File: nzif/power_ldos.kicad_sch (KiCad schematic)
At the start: 62 parts, among them U152 LT3042xMSE, U153 LT3042xMSE, U154 LT3042xMSE, U155 LT3042xMSE, U156 LT3042xMSE, U157 LT3042xMSE, U158 LT3045xMSE, U159 LT3045xMSE, U160 LT3045xMSE, U161 LT3045xMSE, U162 LT3045xMSE, U163 LT3045xMSE, U164 LT3045xMSE

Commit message: Digikey parts for rcv stages
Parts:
- C324, C325, C335: Digikey Part # (none) -> 587-3258-1-ND
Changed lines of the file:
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@@
 			)
 		)
-		(property "Datasheet" "~"
+		(property "Datasheet" "https://mm.digikey.com/Volume0/opasdata/d220001/medias/docus/1231/LMK107BBJ106MALT_SS.pdf"
 			(at 228.6 35.56 0)
 			(effects
@@
 			)
 		)
-		(property "Digikey Part #" ""
+		(property "Digikey Part #" "587-3258-1-ND"
 			(at 228.6 35.56 0)
 			(effects
@@
 			)
 		)
-		(property "Datasheet" "~"
+		(property "Datasheet" "https://mm.digikey.com/Volume0/opasdata/d220001/medias/docus/1231/LMK107BBJ106MALT_SS.pdf"
 			(at 326.39 35.56 0)
 			(effects
@@
 			)
 		)
-		(property "Digikey Part #" ""
+		(property "Digikey Part #" "587-3258-1-ND"
 			(at 326.39 35.56 0)
 			(effects
@@
 			)
 		)
-		(property "Datasheet" "~"
+		(property "Datasheet" "https://mm.digikey.com/Volume0/opasdata/d220001/medias/docus/1231/LMK107BBJ106MALT_SS.pdf"
 			(at 226.06 113.03 0)
 			(effects
@@
 			)
 		)
-		(property "Digikey Part #" ""
+		(property "Digikey Part #" "587-3258-1-ND"
 			(at 226.06 113.03 0)
 			(effects

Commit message: add annotations - first run of erc
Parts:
- renumbered C306 to C312, C307 to C313, C308 to C314, C310 to C315, C309 to C316, C311 to C317, C312 to C318, C313 to C319, C314 to C320, C315 to C321, C316 to C322, C317 to C323, C318 to C324, C319 to C325, C320 to C326, C321 to C327, C322 to C328, C323 to C329, C324 to C330, C325 to C331, C326 to C332, C327 to C333, C328 to C334, C329 to C335, C330 to C336, C331 to C337, C332 to C338, C333 to C339, C334 to C340, C335 to C341, C336 to C342, C337 to C343, C338 to C344, R226 to R194, R225 to R195, R227 to R196, R228 to R197, R229 to R198, R230 to R199, R231 to R200, R232 to R201, R233 to R202, R234 to R203, R235 to R204, R236 to R205, R237 to R206, R238 to R207, R239 to R208, R240 to R209, U152 to U144, U153 to U145, U154 to U146, U155 to U147, U156 to U148, U157 to U149, U158 to U150, U159 to U151, U160 to U152, U161 to U153, U162 to U154, U163 to U155, U164 to U156

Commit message: updated power on all schematics
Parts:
- removed C330, C331: 10u, Capacitor_SMD:C_0603_1608Metric_Pad1.08x0.95mm_HandSolder, symbol Device:C_Small
- removed C332, C333, C335: 0.47u, Capacitor_SMD:C_0603_1608Metric_Pad1.08x0.95mm_HandSolder, symbol Device:C_Small
- removed C334, C336, C337, C338, C339, C340: 4.7u, Capacitor_SMD:C_0603_1608Metric_Pad1.08x0.95mm_HandSolder, symbol Device:C_Small
- removed R200, R201: 16.5k, Resistor_SMD:R_0603_1608Metric_Pad0.98x0.95mm_HandSolder, symbol Device:R_Small_US
- removed R202: 33.2k, Resistor_SMD:R_0603_1608Metric_Pad0.98x0.95mm_HandSolder, symbol Device:R_Small_US
- removed R203, R204, R205, R206: 20m, Resistor_SMD:R_0603_1608Metric_Pad0.98x0.95mm_HandSolder, symbol Device:R_Small_US
- removed U144, U145, U146, U147, U148, U149: LT3042xMSE, Package_SO:MSOP-10-1EP_3x3mm_P0.5mm_EP1.68x1.88mm, symbol Regulator_Linear:LT3042xMSE
- removed U150, U151, U152, U154: LT3045xMSE, Package_SO:MSOP-12-1EP_3x4.039mm_P0.65mm_EP1.651x2.845mm, symbol Regulator_Linear:LT3045xMSE
- added C? (x2): 4.7u, Capacitor_SMD:C_0603_1608Metric_Pad1.08x0.95mm_HandSolder, symbol Device:C_Small
- added C?: 0.47u, Capacitor_SMD:C_0603_1608Metric_Pad1.08x0.95mm_HandSolder, symbol Device:C_Small
- added R?: 49.9, Resistor_SMD:R_0603_1608Metric_Pad0.98x0.95mm_HandSolder, symbol Device:R_Small_US
- added U144, U145, U146, U147, U148, U149: LT3045xMSE, Package_SO:MSOP-12-1EP_3x4.039mm_P0.65mm_EP1.651x2.845mm, symbol Regulator_Linear:LT3045xMSE
- C323, C327: value 4.7u -> 0.47u
- C324, C326: value 0.47u -> 4.7u
- R197: value 33.2k -> 49.9
- R199: value 49.9 -> 49.9k
- renumbered U153 to U?
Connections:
- net 3.3V_DACs is gone; now on an unnamed net: C327.1
- net 5V_RX_OPAMPS is gone; now on net +6.5V_RX_OPAMPS: C320.1
- net GND: now also C?.2, C?.2, C?.2, R?.2, U144.13 (GND), U144.6 (ILIM), U144.9 (GND), U145.13 (GND), U145.6 (ILIM), U145.9 (GND), U146.13 (GND), U146.6 (ILIM), U146.9 (GND), U147.13 (GND), U147.6 (ILIM), U147.9 (GND), U148.13 (GND), U148.6 (ILIM), U148.9 (GND), U149.13 (GND), U149.6 (ILIM), U149.9 (GND)
- net at C317.1, R196.1: now also U?.8 (SET)
- net at R199.1: now also U149.8 (SET); no longer C326.1
- net at R197.1: now also C323.1, U147.8 (SET); no longer C324.1
- net at C316.1, R195.1: now also U148.8 (SET)
- net at C315.1, R194.1: now also U145.8 (SET)
- net at C325.1, R198.1: now also U144.8 (SET)
- net +6.5V_RX_OPAMPS: now reaches U?.10 (OUTS), U?.11 (OUT), U?.12 (OUT)
- net 3.3V_ADCs renamed +3.3V_CONVERTERS
- net +3.3V_CONVERTERS: now also U148.10 (OUTS), U148.11 (OUT), U148.12 (OUT)
- net 3.3V_DSP renamed +3.3V_DSP_UC
- net 3.6V renamed 4V
- net 4V: now also C?.1, U146.1 (IN), U146.2 (IN), U146.3 (IN), U146.4 (EN/UV), U146.7 (PGFB), U147.1 (IN), U147.2 (IN), U147.3 (IN), U147.4 (EN/UV), U147.7 (PGFB), U148.1 (IN), U148.2 (IN), U148.3 (IN), U148.4 (EN/UV), U148.7 (PGFB); no longer C314.1, U?.1 (IN), U?.2 (IN), U?.3 (IN), U?.4 (EN/UV), U?.7 (PGFB)
- net 5.5V renamed 6V
- net 6V: now also C326.1, U144.1 (IN), U144.2 (IN), U144.3 (IN), U144.4 (EN/UV), U144.7 (PGFB), U145.1 (IN), U145.2 (IN), U145.3 (IN), U145.4 (EN/UV), U145.7 (PGFB), U149.1 (IN), U149.2 (IN), U149.3 (IN), U149.4 (EN/UV), U149.7 (PGFB); no longer C323.1
- net 5V_RX_Mixer renamed +5V_RX_MIXER
- net +5V_RX_MIXER: now also U145.10 (OUTS), U145.11 (OUT), U145.12 (OUT)
- net 5V_TX_Mixer renamed +5V_TX_MIXER
- net +5V_TX_MIXER: now also U144.10 (OUTS), U144.11 (OUT), U144.12 (OUT)
- net 5V_TX_OPAMPS renamed +5V_LOUDSPEAKER
- net +5V_LOUDSPEAKER: now also U149.10 (OUTS), U149.11 (OUT), U149.12 (OUT)
- new net: C?.1, R?.1, U146.8 (SET)
- new net +1.8V_CLOCKTREE: C?.1, U146.10 (OUTS), U146.11 (OUT), U146.12 (OUT)
- new net +3.3V_CLOCKTREE: C324.1, U147.10 (OUTS), U147.11 (OUT), U147.12 (OUT)
- new net 8V: C314.1, U?.1 (IN), U?.2 (IN), U?.3 (IN), U?.4 (EN/UV), U?.7 (PGFB)
- no-connect marks 13 -> 9
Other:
- note added: "3.3V Power for ADCs/DACs/Codec"
- note added: "3.3V Power for DSP and uC"
- note added: "5V Power for Loudspeaker"
- note added: "6.5V Power for RX op amps"
- note added: "Resistor sets 1.8V output Use high quality cap such as COG"
- note added: "Resistor sets 6.5V output Use high quality cap such as COG"
- note removed: "3.3V Power for ADCs"
- note removed: "3.3V Power for DACs"
- note removed: "3.3V Power for DSP"
- note removed: "3.3V Power for Microcontroller"
- note removed: "5V Power for RX op amps"
- note removed: "5V Power for TX Op amps"
- moved on the sheet: U?

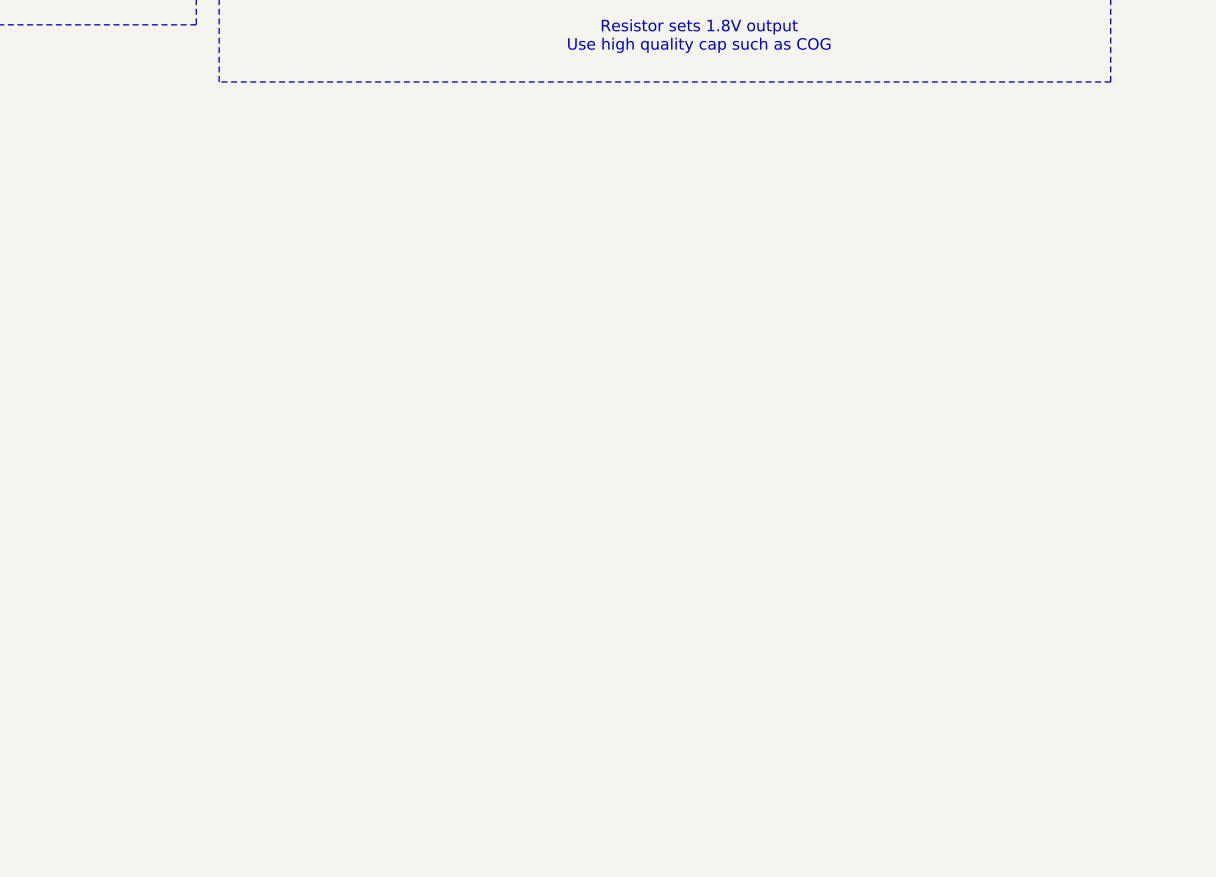
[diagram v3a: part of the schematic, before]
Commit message: added ldo for 2.5V
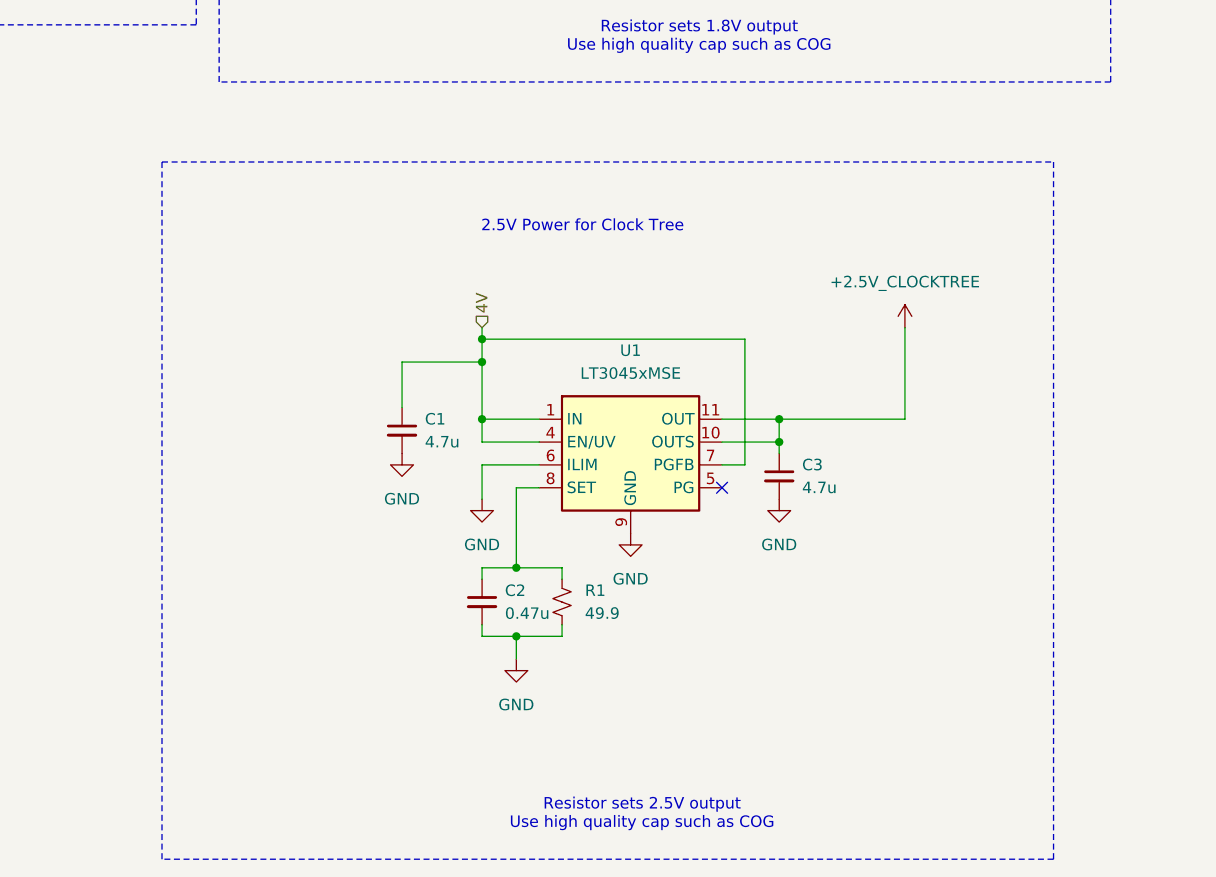
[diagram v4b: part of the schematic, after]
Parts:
- added C1, C3: 4.7u, Capacitor_SMD:C_0603_1608Metric_Pad1.08x0.95mm_HandSolder, symbol Device:C_Small
- added C2: 0.47u, Capacitor_SMD:C_0603_1608Metric_Pad1.08x0.95mm_HandSolder, symbol Device:C_Small
- added R1: 49.9, Resistor_SMD:R_0603_1608Metric_Pad0.98x0.95mm_HandSolder, symbol Device:R_Small_US
- added U1: LT3045xMSE, Package_SO:MSOP-12-1EP_3x4.039mm_P0.65mm_EP1.651x2.845mm, symbol Regulator_Linear:LT3045xMSE
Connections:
- net 4V: now also C1.1, U1.1 (IN), U1.2 (IN), U1.3 (IN), U1.4 (EN/UV), U1.7 (PGFB)
- net GND: now also C1.2, C2.2, C3.2, R1.2, U1.13 (GND), U1.6 (ILIM), U1.9 (GND)
- new net: C2.1, R1.1, U1.8 (SET)
- new net +2.5V_CLOCKTREE: C3.1, U1.10 (OUTS), U1.11 (OUT), U1.12 (OUT)
- no-connect marks 9 -> 10
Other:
- note added: "2.5V Power for Clock Tree"
- note added: "Resistor sets 2.5V output Use high quality cap such as COG"

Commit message: cartoons on main2
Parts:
- renumbered C1 to C?, C3 to C?, C2 to C?, R1 to R?, U1 to U?

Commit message: wire top sheet from rf front end through rx driver amps
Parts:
- gave numbers to parts that had none: 10
- renumbered C312 to C901, C313 to C902, C314 to C903, C315 to C904, C316 to C905, C317 to C906, C318 to C907, C319 to C908, C320 to C909, C322 to C910, C326 to C911, C325 to C912, C327 to C913, C328 to C914, C329 to C915, C321 to C917, C323 to C920, C324 to C923, C341 to C925, C342 to C926, C343 to C927, C344 to C928, R194 to R901, R195 to R902, R196 to R903, R198 to R904, R199 to R905, R197 to R907, R207 to R909, R208 to R910, R209 to R911, U148 to U901, U145 to U902, U144 to U904, U149 to U905, U147 to U907, U146 to U908, U155 to U909, U156 to U910

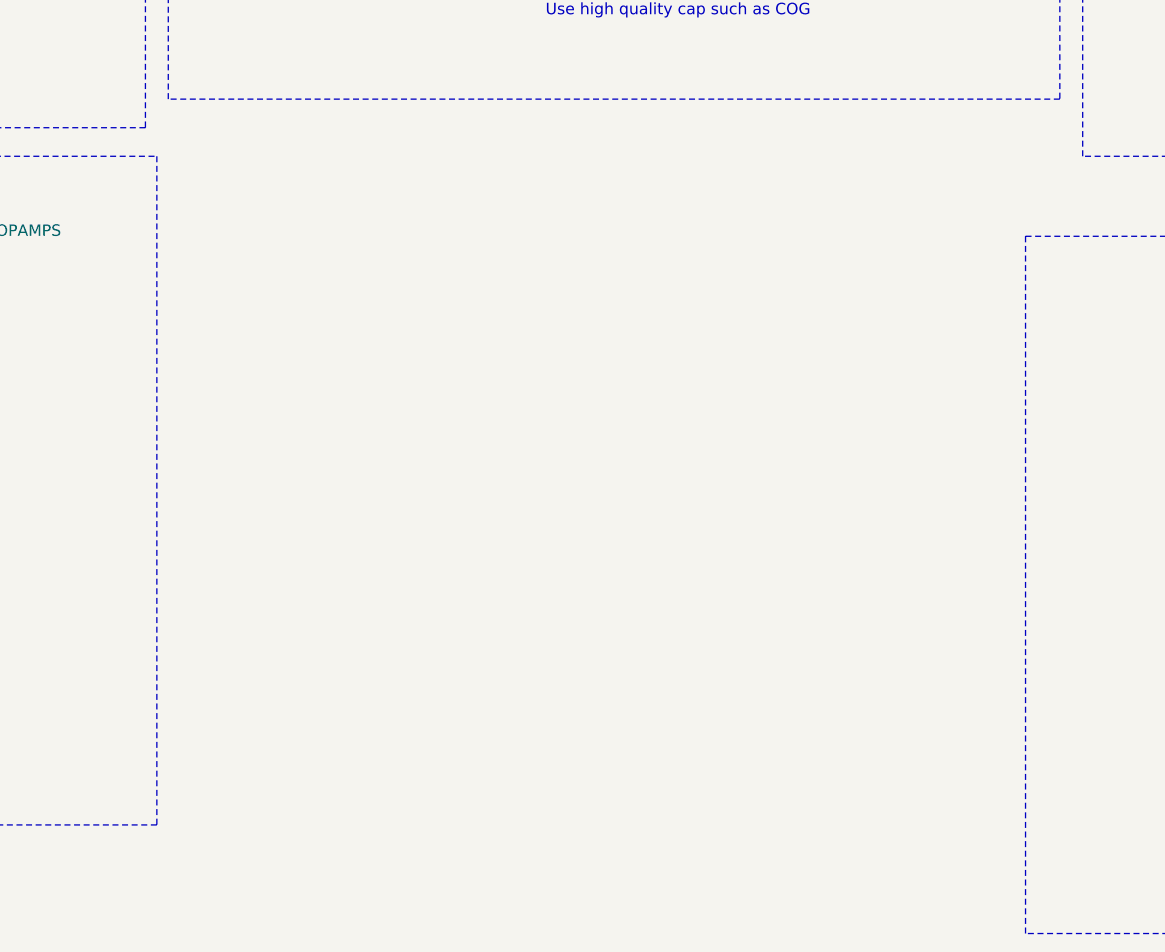
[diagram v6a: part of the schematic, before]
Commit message: added -3.5V rail
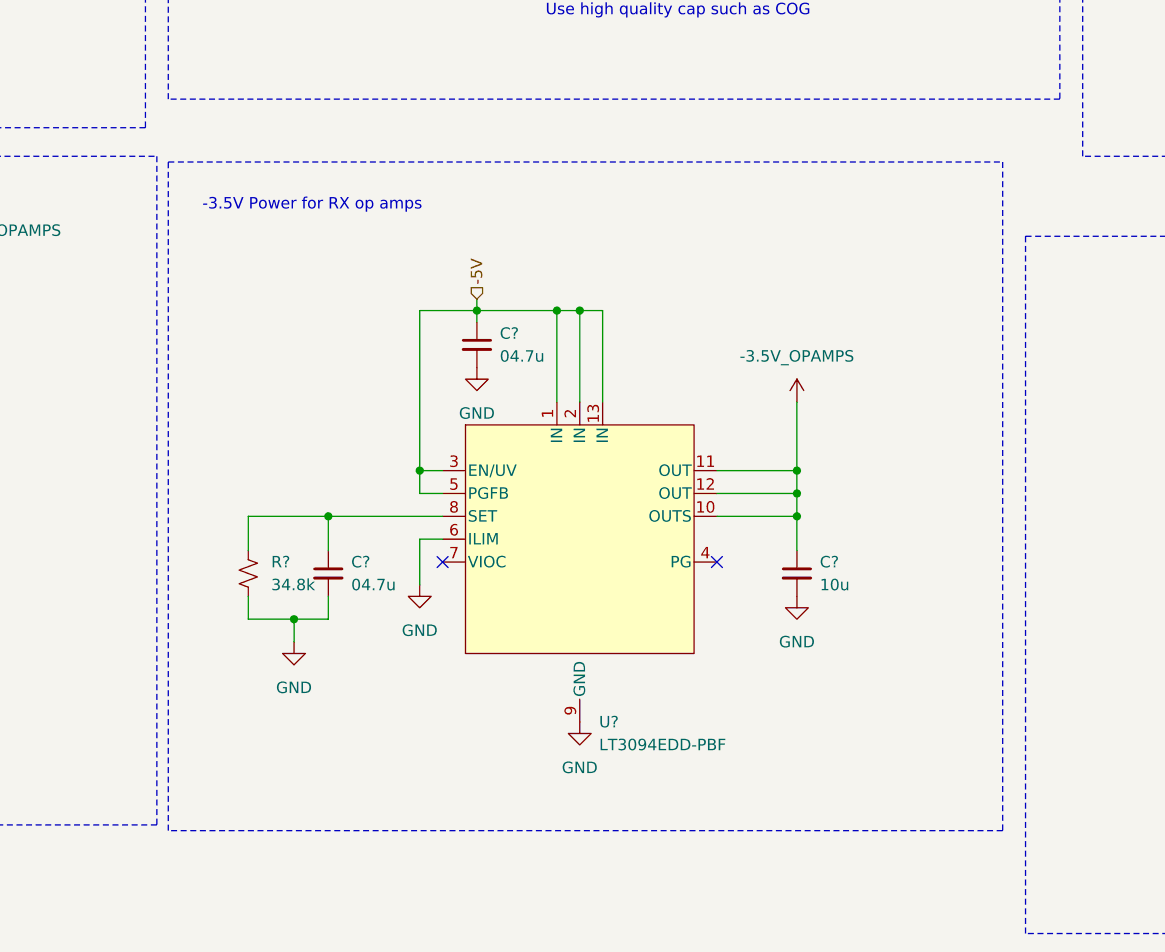
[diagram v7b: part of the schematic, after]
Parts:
- added C?: 10u, Capacitor_SMD:C_0603_1608Metric_Pad1.08x0.95mm_HandSolder, symbol Device:C_Small
- added C? (x2): 04.7u, Capacitor_SMD:C_0603_1608Metric_Pad1.08x0.95mm_HandSolder, symbol Device:C_Small
- added R?: 34.8k, symbol Device:R_Small_US
- added U?: LT3094EDD-PBF, nzif_footprints:DD_05-08-1725_ADI, symbol nzif_radio_symbol_library:LT3094EDD-PBF
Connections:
- net GND: now also C?.2, C?.2, C?.2, R?.2, U?.6 (ILIM), U?.9 (GND)
- new net: C?.1, R?.1, U?.8 (SET)
- new net -3.5V_OPAMPS: C?.1, U?.10 (OUTS), U?.11 (OUT), U?.12 (OUT)
- new net -5V: C?.1, U?.1 (IN), U?.13 (IN), U?.2 (IN), U?.3 (EN/UV), U?.5 (PGFB)
- no-connect marks 10 -> 12
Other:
- note added: "-3.5V Power for RX op amps"
